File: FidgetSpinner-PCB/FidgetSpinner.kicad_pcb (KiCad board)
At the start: 2 copper layers, 80.5 x 88.6 mm, 38 parts, among them J1 Holes, Q1 Q_Photo_NPN, SW1 SW_SPST, SW2 button, U1 ATmega328P-AU, Y1 16M

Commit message: fixed: CR2477 label
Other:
- board text added: "CR2477 x3"
- board text removed: "CR2032 x3"

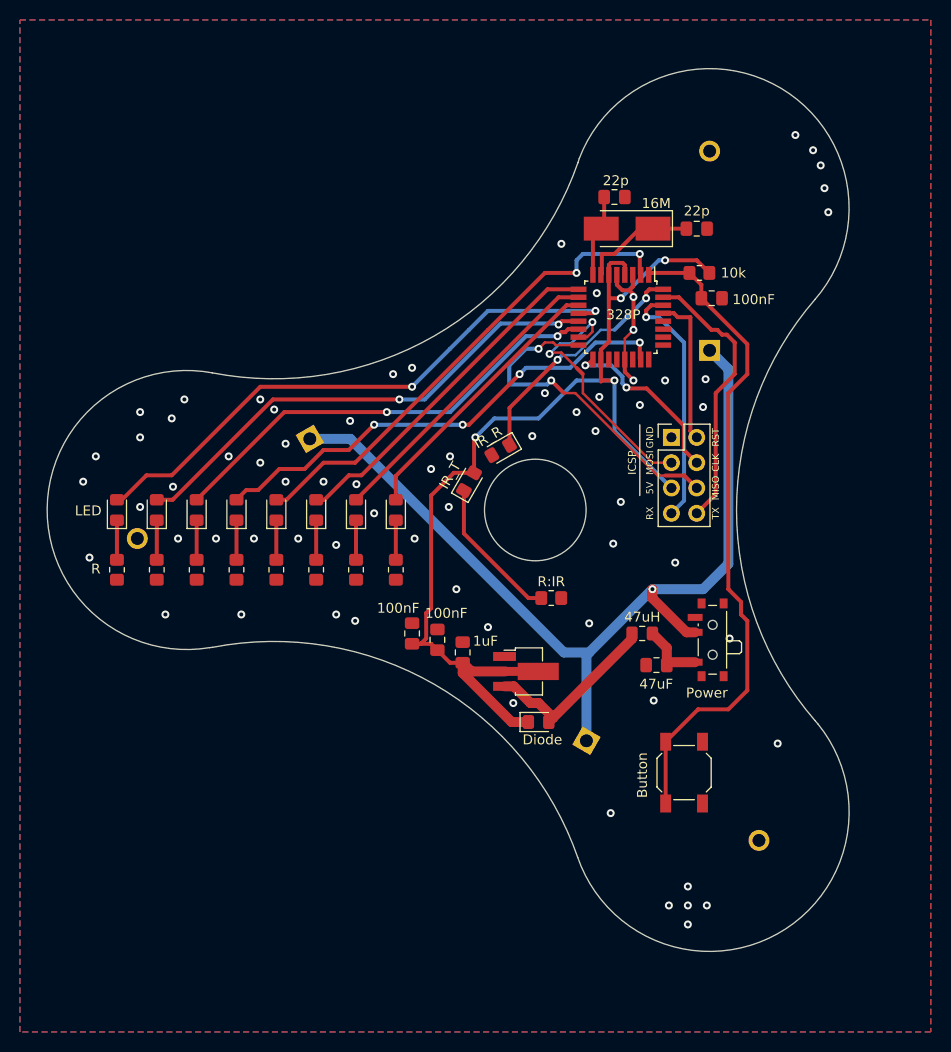
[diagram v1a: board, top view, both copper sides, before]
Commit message: changed to STM32 and CR2450
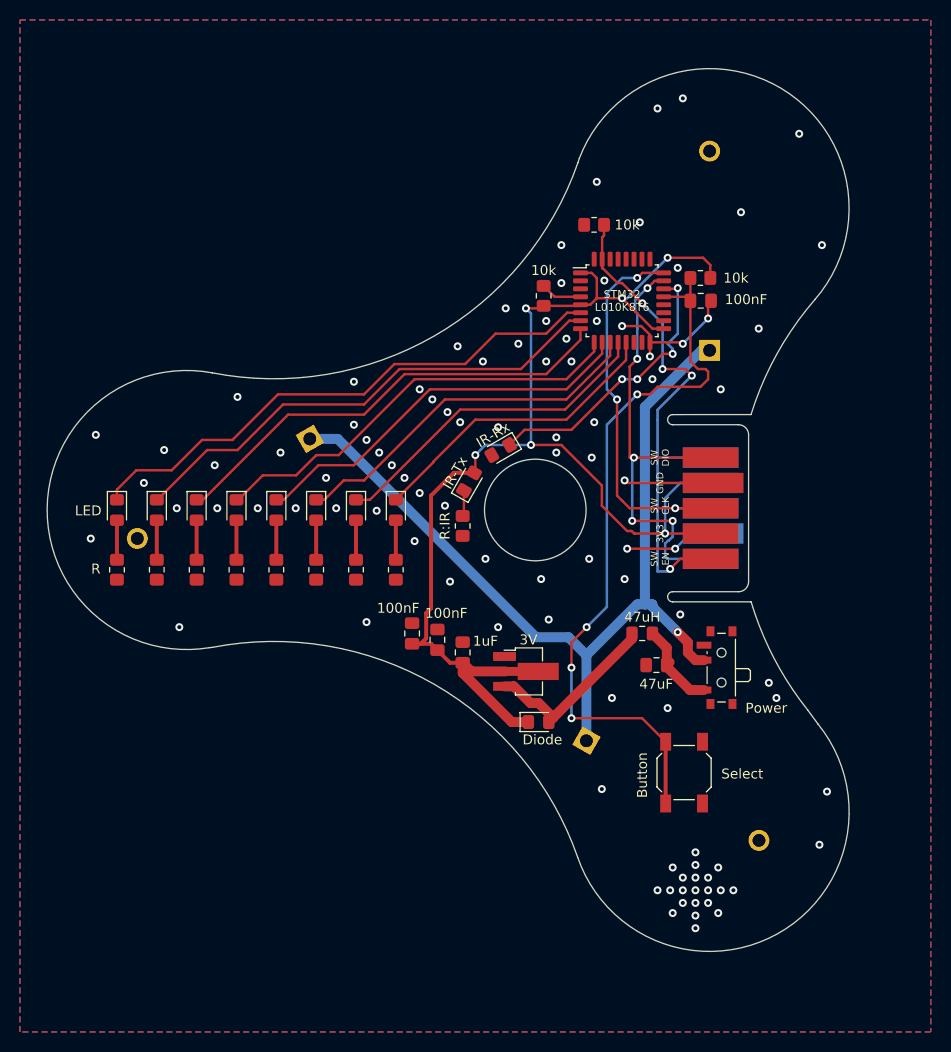
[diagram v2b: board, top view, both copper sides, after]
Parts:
- removed C1, C2: 22p, Capacitor_SMD:C_0805_2012Metric_Pad1.18x1.45mm_HandSolder
- removed Y1: 16M, Crystal:Crystal_SMD_5032-2Pin_5.0x3.2mm_HandSoldering
- added R11: 10k, Resistor_SMD:R_0805_2012Metric_Pad1.20x1.40mm_HandSolder, F.Cu at (105.9, 71.4)
- added R12: 10k, Resistor_SMD:R_0805_2012Metric_Pad1.20x1.40mm_HandSolder, F.Cu at (100.8, 78.5)
- BT1, BT2, BT3: footprint Battery:BatteryHolder_ComfortableElectronic_CH273-2450_1x2450 -> WYW_Package:CR2450_Centered
- J1: value Holes -> EdgeConnector; footprint Connector_PinHeader_2.54mm:PinHeader_2x04_P2.54mm_Vertical -> WYW_Package:Edge_2x05_2.54
- SW1: value SW_SPST -> SW_POWER
- U1: value ATmega328P-AU -> STM32L010K8T6; footprint Package_QFP:TQFP-32_7x7mm_P0.8mm -> Package_QFP:LQFP-32_7x7mm_P0.8mm
- moved R10 11.5 mm to (92.7, 101.6), turned to 90 degrees
- moved J1 9.45 mm to (119.9, 99.8), turned to 90 degrees
- moved SW1 2.93 mm to (118.4, 115.8)
- moved U1 1.66 mm to (108.7, 79.0), turned to 0 degrees
- moved C8 1.13 mm to (116.6, 79.0)
- moved R9 0.52 mm to (116.6, 76.7)
- turned D10 to 270 degrees
- turned D11 to 270 degrees
- turned D12 to 270 degrees
- turned D13 to 270 degrees
- turned D14 to 270 degrees
- turned D15 to 270 degrees
- turned D16 to 270 degrees
- turned D17 to 270 degrees
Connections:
- net TX renamed SWEN
- D10 pad 1: Net-(D10-Pad1) -> L0
- D10 pad 2: L0 -> Net-(D10-Pad2)
- D11 pad 1: Net-(D11-Pad1) -> L1
- D11 pad 2: L1 -> Net-(D11-Pad2)
- D12 pad 1: Net-(D12-Pad1) -> L2
- D12 pad 2: L2 -> Net-(D12-Pad2)
- D13 pad 1: Net-(D13-Pad1) -> L3
- D13 pad 2: L3 -> Net-(D13-Pad2)
- D14 pad 1: Net-(D14-Pad1) -> L4
- D14 pad 2: L4 -> Net-(D14-Pad2)
- D15 pad 1: Net-(D15-Pad1) -> L5
- D15 pad 2: L5 -> Net-(D15-Pad2)
- D16 pad 1: Net-(D16-Pad1) -> L6
- D16 pad 2: L6 -> Net-(D16-Pad2)
- D17 pad 1: Net-(D17-Pad1) -> L7
- D17 pad 2: L7 -> Net-(D17-Pad2)
- J1 pad 1: GND -> SWDIO
- J1 pad 2: MOSI -> GND
- J1 pad 3: VCC -> SWCLK
- J1 pad 4: RX -> VCC
- R1 pad 2: Net-(D10-Pad1) -> Net-(D10-Pad2)
- R2 pad 2: Net-(D11-Pad1) -> Net-(D11-Pad2)
- R3 pad 2: Net-(D12-Pad1) -> Net-(D12-Pad2)
- R4 pad 2: Net-(D13-Pad1) -> Net-(D13-Pad2)
- R5 pad 2: Net-(D14-Pad1) -> Net-(D14-Pad2)
- R6 pad 2: Net-(D15-Pad1) -> Net-(D15-Pad2)
- R7 pad 2: Net-(D16-Pad1) -> Net-(D16-Pad2)
- R8 pad 2: Net-(D17-Pad1) -> Net-(D17-Pad2)
- U1 pad 1: INT_B -> VCC
- U1 pad 10: L6 -> L4
- U1 pad 11: L7 -> L5
- U1 pad 12: L0 -> L6
- U1 pad 13: L1 -> L7
- U1 pad 14: L2 -> Net-(U1-Pad14)
- U1 pad 15: MOSI -> Net-(U1-Pad15)
- U1 pad 16: MISO -> GND
- U1 pad 17: CLK -> VCC
- U1 pad 18: VCC -> Net-(U1-Pad18)
- U1 pad 2: L4 -> Net-(U1-Pad2)
- U1 pad 21: GND -> INT_B
- U1 pad 22: Net-(U1-Pad22) -> ~INT_C
- U1 pad 23: L3 -> SWDIO
- U1 pad 24: Net-(U1-Pad24) -> SWCLK
- U1 pad 29: RST -> Net-(U1-Pad29)
- U1 pad 3: GND -> Net-(U1-Pad3)
- U1 pad 30: RX -> Net-(U1-Pad30)
- U1 pad 32: ~INT_C -> GND
- U1 pad 4: VCC -> Net-(R12-Pad1)
- U1 pad 5: GND -> VCC
- U1 pad 6: VCC -> L0
- U1 pad 7: Net-(C1-Pad2) -> L1
- U1 pad 8: Net-(C2-Pad2) -> L2
- U1 pad 9: L5 -> L3
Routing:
- net SWDIO: track 0.00 -> 47.1 mm, vias 0 -> 5
- net SWCLK: track 0.00 -> 40.8 mm, vias 0 -> 3
- net MISO: track 33.4 -> 0.00 mm, vias 2 -> 0
- net MOSI: track 26.2 -> 0.00 mm, vias 2 -> 0
- net SWEN: track 27.8 -> 53.2 mm, vias 0 -> 4
- net RX: track 25.1 -> 0.00 mm, vias 1 -> 0
- net VCC: track 102.5 -> 125.7 mm, vias 4 -> 6
- net GND: track 14.1 -> 32.4 mm, vias 69 -> 100
- net CLK: track 18.1 -> 0.00 mm, vias 2 -> 0
- net RST: track 15.2 -> 0.00 mm
- net Net-(D2-Pad1): track 14.8 -> 2.61 mm
- net Net-(C1-Pad2): track 11.7 -> 0.00 mm
- net L4: track 49.6 -> 39.9 mm, vias 2 -> 0
- net Net-(C2-Pad2): track 8.28 -> 0.00 mm
- net INT_B: track 66.6 -> 73.8 mm, vias 0 -> 4
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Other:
- outline, holes or cut-outs redrawn
- board text added: "3V"
- board text added: "3V3"
- board text added: "CR2450 x3"
- board text added: "IR-Rx"
- board text added: "IR-Tx"
- board text added: "PhOVS FidgetSpinner v0.2.0 - (C) WYW 2021-11-04"
- board text added: "STM32 L010K8T6"
- board text added: "SW CLK"
- board text added: "SW DIO"
- board text added: "SW EN"
- board text added: "Select"
- board text removed: "16M"
- board text removed: "22p"
- board text removed: "328P"
- board text removed: "5V"
- board text removed: "CLK"
- board text removed: "CR2477 x3"
- board text removed: "FidgetSpinner-LED v0.1.0 - (C) WYW 2021-11-04"
- board text removed: "ICSP"
- board text removed: "IR_R"
- board text removed: "IR_T"
- board text removed: "MISO"
- board text removed: "MOSI"
- board text removed: "RST"
- board text removed: "RX"
- board text removed: "TX"

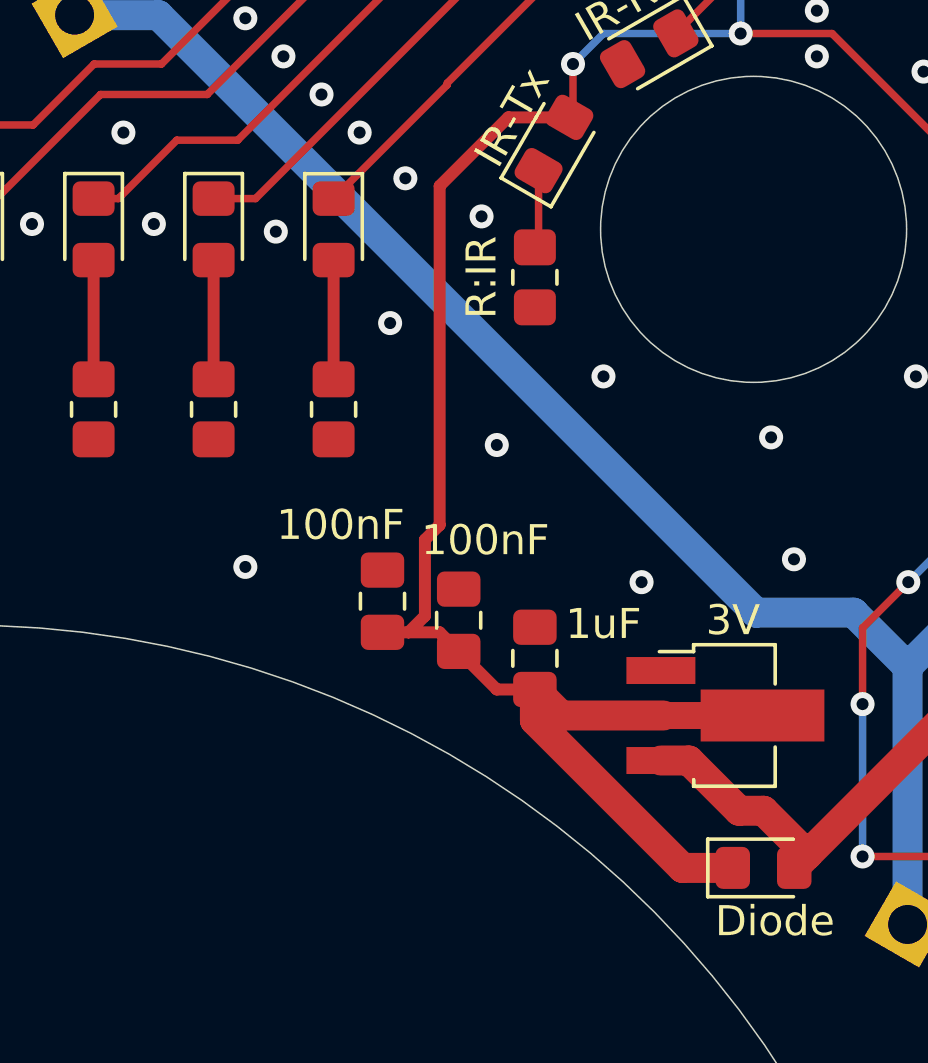
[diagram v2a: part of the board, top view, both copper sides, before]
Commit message: button animations
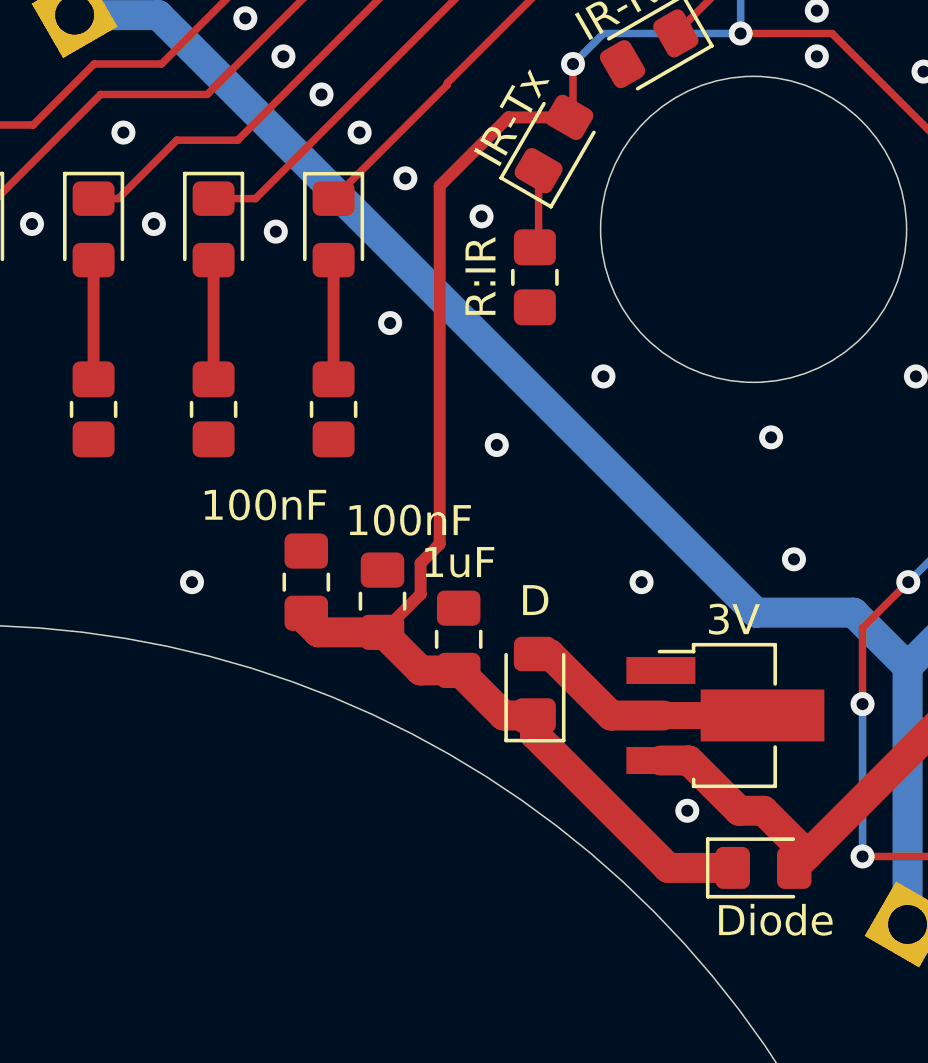
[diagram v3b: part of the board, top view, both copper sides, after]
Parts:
- added D3: D, Diode_SMD:D_0805_2012Metric_Pad1.15x1.40mm_HandSolder, F.Cu at (92.7, 115.2)
- HS1: value BL8530-50 -> BL8530-30
- moved C5 2.62 mm to (87.6, 112.4)
- moved C4 2.62 mm to (90.2, 113.7)
- moved C6 2.62 mm to (85.1, 111.8)
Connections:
- net Net-(C3-Pad1) renamed VBAT
- HS1 pad 2: VCC -> Net-(D3-Pad2)
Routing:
- net Net-(D3-Pad2): track 0.00 -> 5.14 mm
- net VCC: track 125.7 -> 124.1 mm
- net GND: vias 100 -> 101
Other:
- board text added: "D"
